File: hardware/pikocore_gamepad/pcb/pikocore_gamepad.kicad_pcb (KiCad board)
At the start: 4 copper layers, 100 x 80 mm, 72 parts, among them J1 PHONES, J4 LCD_FPC, J5 SPEAKER 8R, Q1 2N7002, SW1 DPAD_UP, SW10 BTN_R, SW11 BTN_START, SW12 BTN_SELECT, SW15 PWR, SW2 DPAD_DOWN, SW3 DPAD_LEFT, SW4 DPAD_RIGHT, SW5 BTN_X, SW6 BTN_Y, SW7 BTN_A, SW8 BTN_B, SW9 BTN_L, U1 RP2350-Plus-16MB, U2 TPS61023DRLR, U3 PT2308-S, U4 PAM8302A, U5 PCM5102APWR

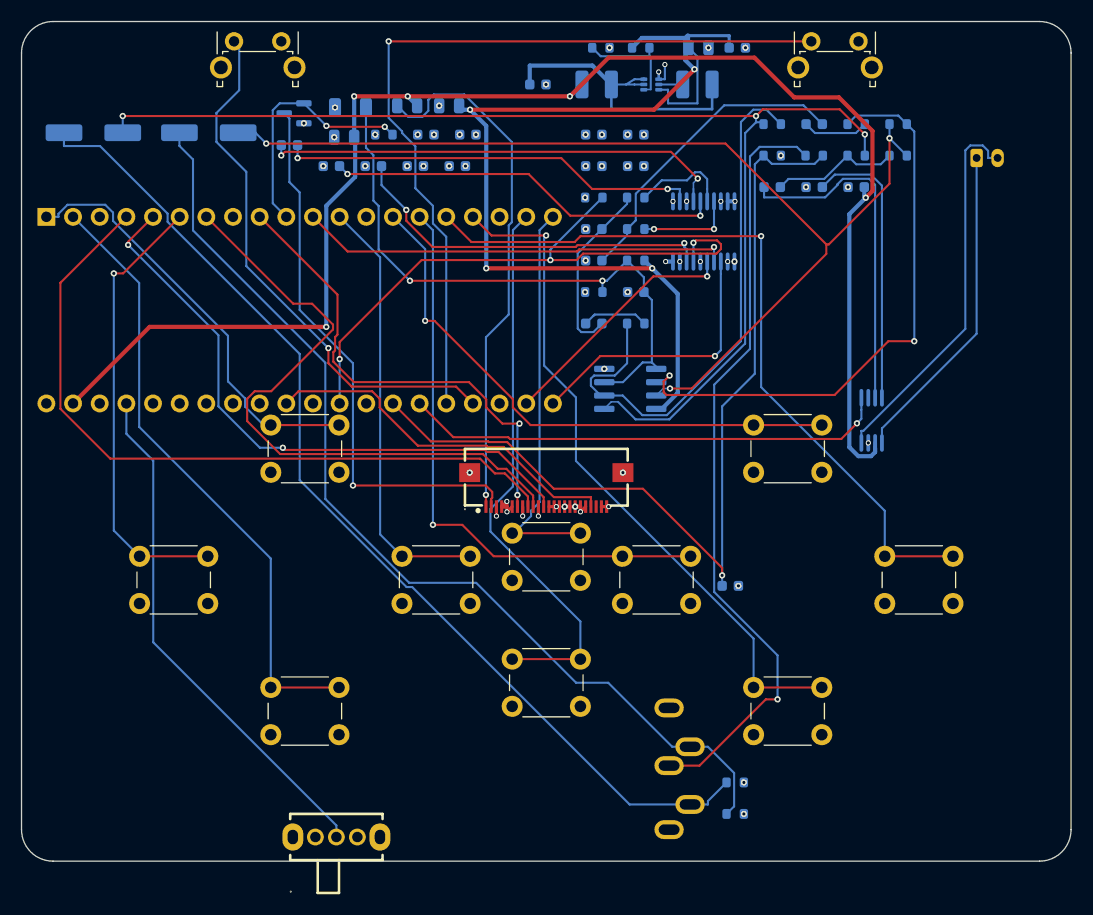
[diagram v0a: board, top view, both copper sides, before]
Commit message: hw: frente Micro y dorso con el modulo plano en 100x60
Frente portado de hw/chipdown-rp2350 (LCD1, J4, SW1-SW15). Dorso: U1 en
MODULE_POS (50,33) rot 0 con flip (pad 1 hacia el borde inferior, USB-C
abajo), J6/J7 arriba en x 33/67, J1 por el borde izquierdo (3,45) rot 270,
MIDI, audio y 470uF en las franjas libres, y el lazo del boost movido
rigido (+29,+50). FREE_REGIONS nuevas para 100x60, fuera de MODULE_BOX.

check_placement.py marca pads pasantes bajo el modulo (TACTO BAJO EL
MODULO). plane_vias.py no pone vias dentro de areas que las prohiben (los
keepouts de los pads de prueba del modulo, detras de J4).

Co-Authored-By: Claude Opus 5.5 <noreply@anthropic.com>
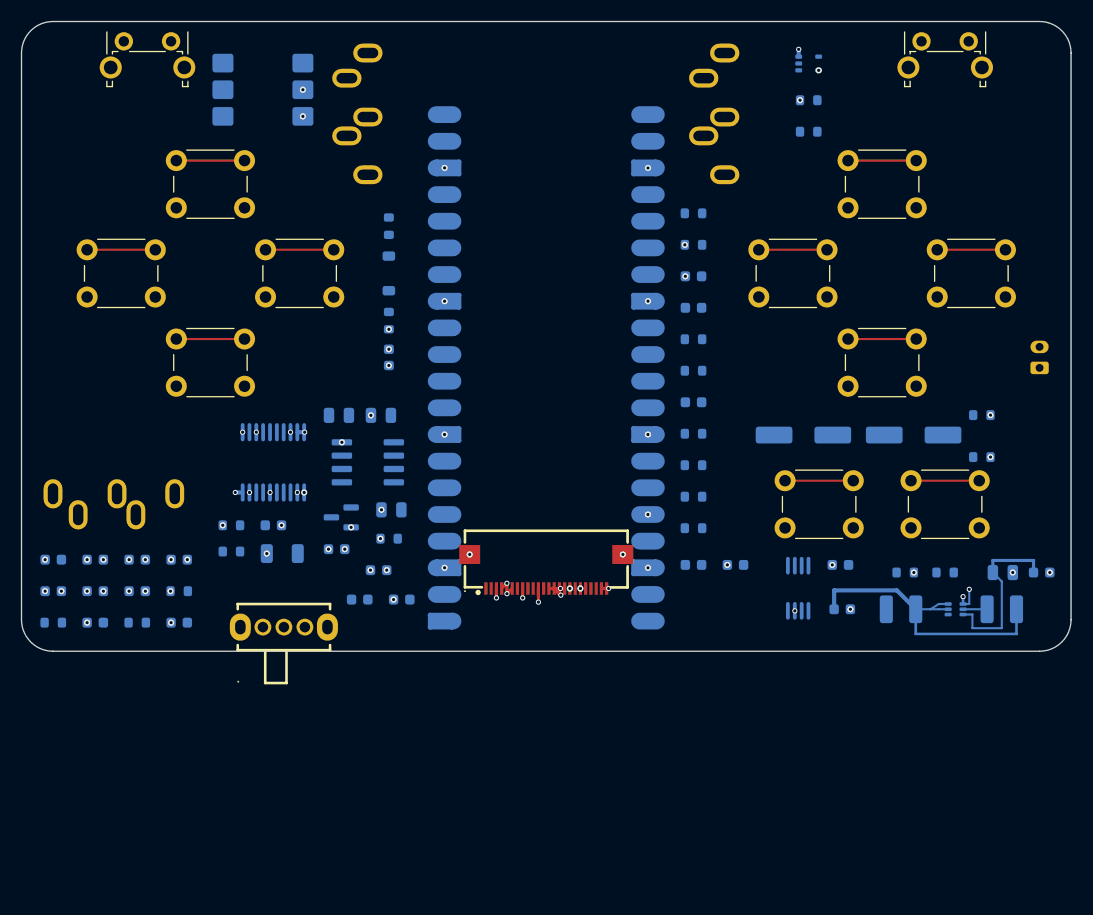
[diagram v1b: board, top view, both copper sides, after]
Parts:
- added C56: 100nF, Capacitor_SMD:C_0603_1608Metric, B.Cu at (35.0, 32.0)
- added D3: 1N4148W, Diode_SMD:D_SOD-123, B.Cu at (35.0, 24.0)
- added J6: MIDI IN, Connector_Audio:Jack_3.5mm_CUI_SJ1-3535NG_Horizontal, B.Cu at (33.0, 3.00)
- added J7: MIDI OUT, Connector_Audio:Jack_3.5mm_CUI_SJ1-3535NG_Horizontal, B.Cu at (67.0, 3.00)
- added R40: 33R, Resistor_SMD:R_0603_1608Metric, B.Cu at (75.0, 7.50)
- added R41: 10R, Resistor_SMD:R_0603_1608Metric, B.Cu at (75.0, 10.5)
- added R42: 220R, Resistor_SMD:R_0603_1608Metric, B.Cu at (35.0, 19.5)
- added R43: 4.7k, Resistor_SMD:R_0603_1608Metric, B.Cu at (35.0, 28.5)
- added U10: H11L1SR2M, Package_DIP:SMDIP-6_W7.62mm, B.Cu at (23.0, 6.50)
- added U9: SN74LVC1G17DCKR, Package_TO_SOT_SMD:SOT-353_SC-70-5, B.Cu at (75.0, 4.00)
- U1: footprint gamesetup_fp:RP2350-Plus_Socket -> gamesetup_fp:RP2350-Plus_Castellated
- moved C23 73.5 mm to (74.5, 39.4), turned to 0 degrees
- moved C24 73.1 mm to (85.0, 39.4), turned to 0 degrees
- moved C14 70.5 mm to (3.02, 54.3)
- moved R7 68.7 mm to (3.02, 57.3)
- moved R18 67.1 mm to (20.0, 50.5), turned to 0 degrees
- moved J1 66.9 mm to (3.00, 45.0), turned to -90 degrees
- moved C15 62.4 mm to (7.03, 54.3)
- moved C16 62.4 mm to (11.0, 54.3)
- moved R15 62.4 mm to (20.0, 48.0), turned to 0 degrees
- moved C17 60.5 mm to (7.03, 57.3)
- moved R8 60.5 mm to (11.0, 57.3)
- moved C4 57.8 mm to (78.2, 56.0)
- moved C5 57.8 mm to (93.5, 52.5)
- moved C7 57.8 mm to (97.2, 52.5)
- moved L1 57.8 mm to (93.4, 56.0)
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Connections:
- U1 pad 32: EXP_GP27 -> MIDI_RX
- U1 pad 34: EXP_GP28 -> MIDI_TX
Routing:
- net VSYS: track 143.0 -> 0.00 mm, vias 5 -> 0
- net AUDIO_L: track 115.9 -> 0.00 mm, vias 3 -> 0
- net AUDIO_R: track 99.6 -> 0.00 mm, vias 3 -> 0
- net JACK_L: track 99.0 -> 0.00 mm
- net JACK_R: track 94.6 -> 0.00 mm
- net JACK_DET: track 87.5 -> 0.00 mm, vias 1 -> 0
- net 5V: track 98.4 -> 16.8 mm, vias 4 -> 0
- net BTN_R: track 77.0 -> 0.00 mm, vias 1 -> 0
- net JACK_DETSW: track 74.6 -> 0.00 mm, vias 1 -> 0
- net LCD_SCK: track 69.9 -> 0.00 mm
- net BTN_A: track 73.1 -> 6.50 mm, vias 1 -> 0
- net LCD_DC: track 61.1 -> 0.00 mm
- net BTN_B: track 65.6 -> 6.50 mm, vias 1 -> 0
- net DAC_XSMT: track 59.0 -> 0.00 mm, vias 3 -> 0
- net LCD_MOSI: track 58.1 -> 0.00 mm, vias 2 -> 0
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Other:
- board size 100 x 80 mm -> 100 x 60 mm

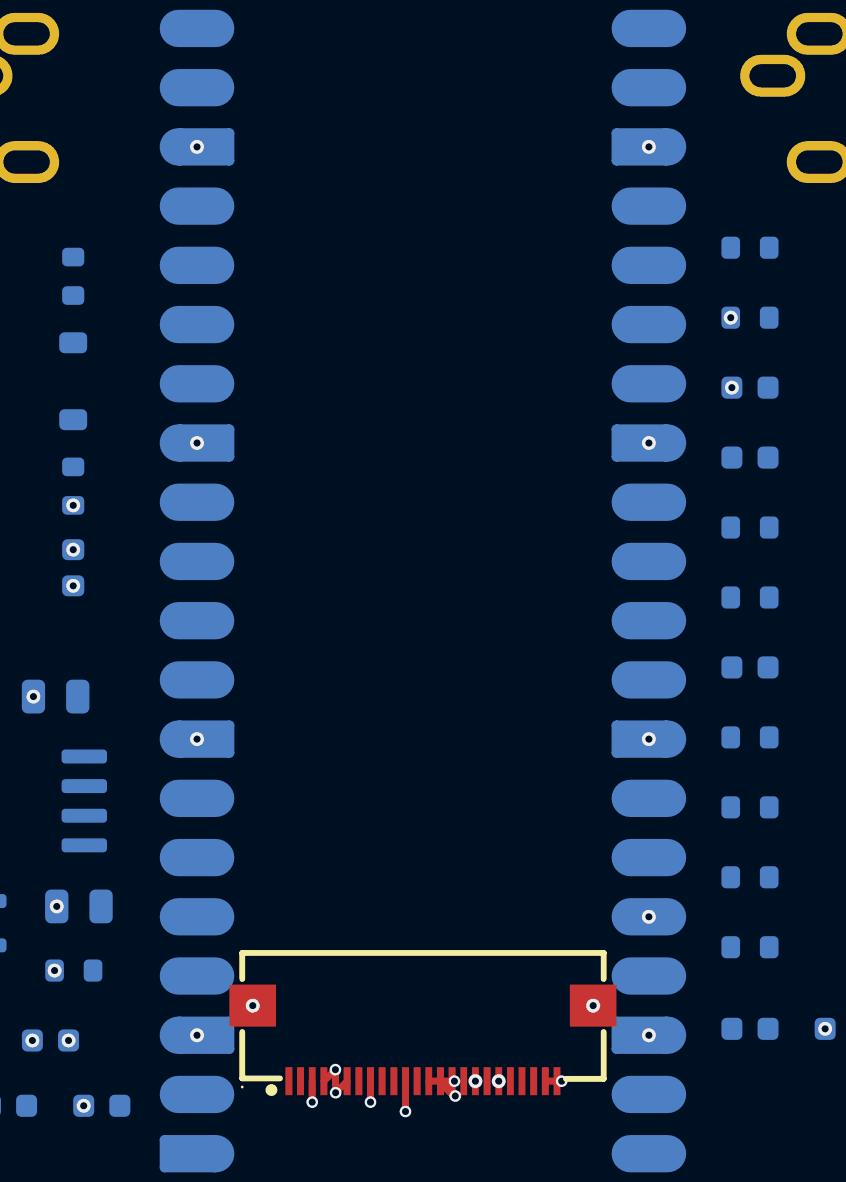
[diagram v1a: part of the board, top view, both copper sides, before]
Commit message: hw: sin vias ni pasta bajo las pastillas del modulo
plane_vias.py ya no pone via en las pastillas de U1 (se sueldan a mano y
el taladro chupa el estano): la via va afuera de la caja de sus pastillas,
a 0.3mm del cobre, unida por un tramo en B.Cu. check_placement.py falla si
una via toca una pastilla de U1.

gen_fp.py quita la pasta sin nombre que la huella oficial traia para
D1-D3 (bajo el modulo el esten imprimiria bolitas). Test de las 40 pastas.

Esquematico y netlist regenerados (U1 ya con la huella castellated).

Co-Authored-By: Claude Opus 5.5 <noreply@anthropic.com>
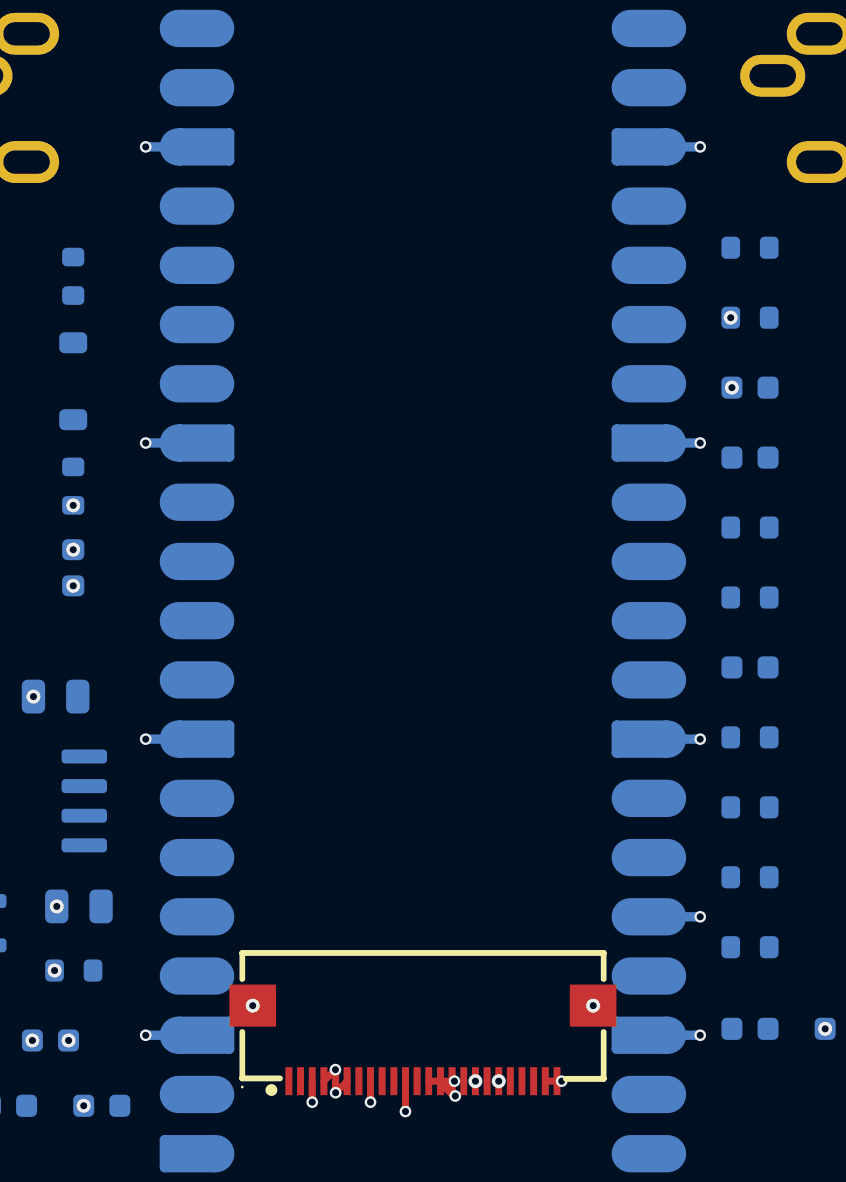
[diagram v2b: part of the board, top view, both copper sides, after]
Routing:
- net GND: track 9.89 -> 27.5 mm
- net 3V3: track 2.10 -> 4.30 mm

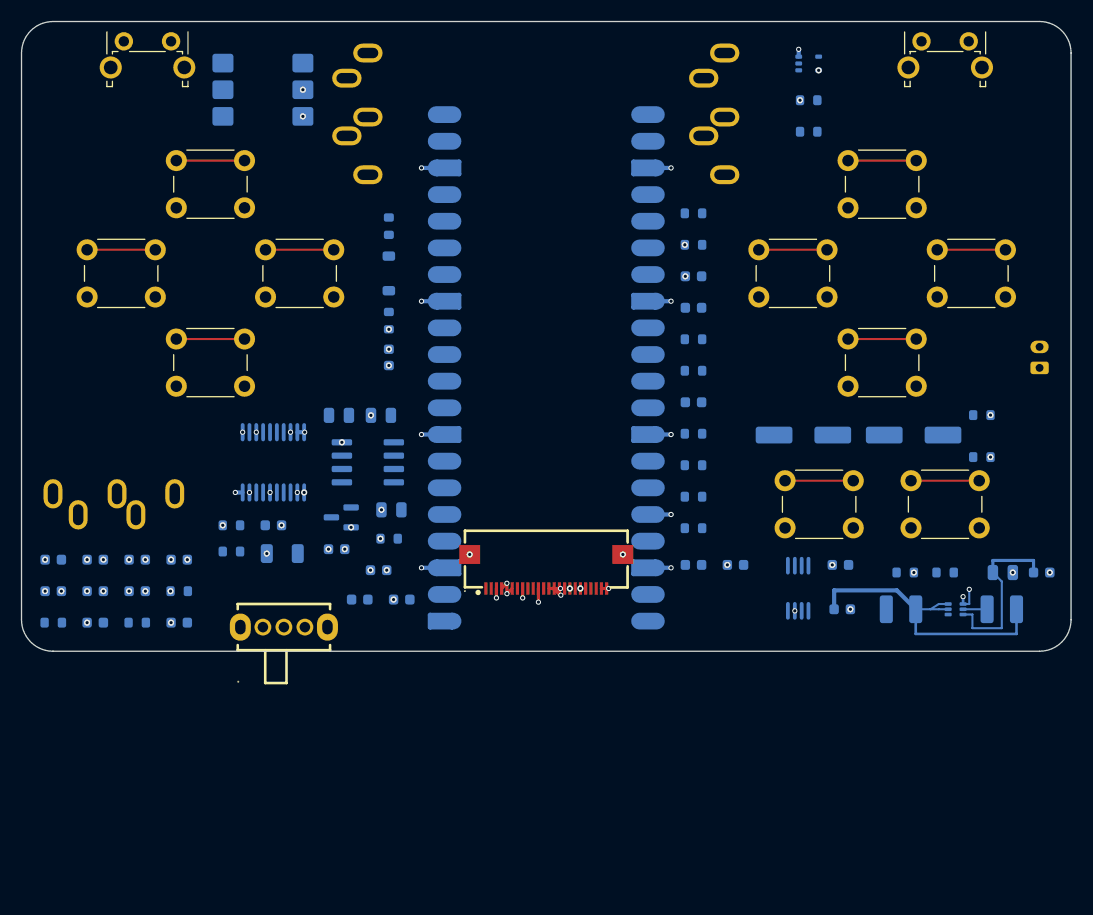
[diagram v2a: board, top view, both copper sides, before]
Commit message: hw: ruteo de la placa con modulo (DRC 0 errores, 0 sin conectar)
Un solo ciclo de route_cycle.sh: freerouting cierra todo en la pasada 1
(696 pistas, 166 vias). DRC: 0 errores, 15 avisos (serigrafia en borde,
lib_footprint_mismatch de SW9/SW10, serigrafia de C23/C24), 0 sin
conectar, 0 de paridad. 5V va en 0.4mm hasta el op-amp sin pista a mano.

check_placement.py mide la via contra la pastilla de U1 como circulo
contra rectangulo: la caja inflada daba falso positivo en las esquinas
(via de BTN_Y a 0.07mm del extremo interior de U1.15, sin tocarla).

Co-Authored-By: Claude Opus 5.5 <noreply@anthropic.com>
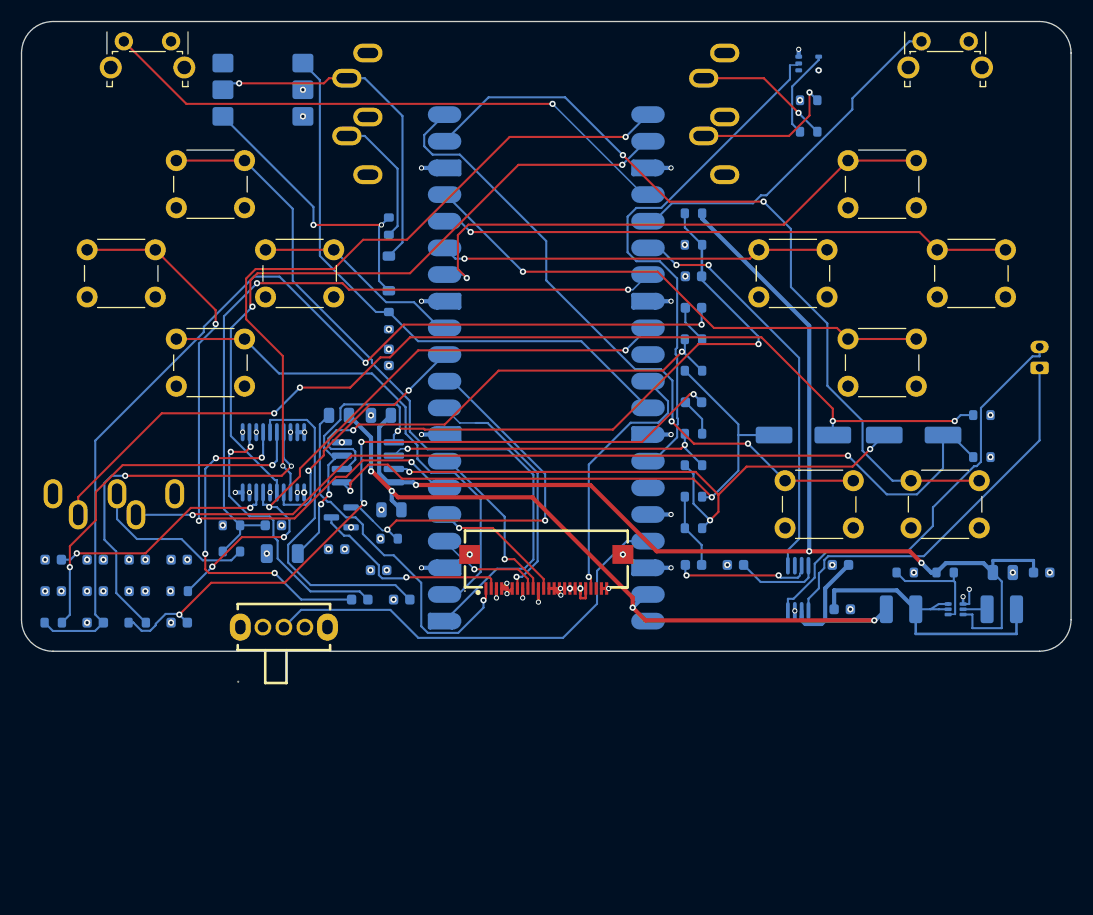
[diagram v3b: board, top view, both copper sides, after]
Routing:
- net 5V: track 16.8 -> 122.4 mm, vias 0 -> 3
- net JACK_L: track 0.00 -> 98.8 mm, vias 0 -> 4
- net AOUT_L: track 0.00 -> 95.0 mm, vias 0 -> 2
- net JACK_R: track 0.00 -> 88.7 mm, vias 0 -> 2
- net VREF25: track 0.00 -> 83.0 mm, vias 0 -> 4
- net VSYS: track 0.00 -> 80.7 mm, vias 0 -> 4
- net BTN_START: track 6.50 -> 76.2 mm, vias 0 -> 2
- net AOUT_R: track 0.00 -> 69.6 mm, vias 0 -> 4
- net JACK_DET: track 0.00 -> 68.7 mm, vias 0 -> 2
- net I2S_BCK: track 0.00 -> 66.9 mm, vias 0 -> 2
- net I2S_LRCK: track 0.00 -> 66.4 mm, vias 0 -> 2
- net DPAD_UP: track 6.50 -> 71.3 mm
- net DAC_XSMT: track 0.00 -> 61.0 mm, vias 0 -> 4
- net AUDIO_R: track 0.00 -> 60.2 mm, vias 0 -> 3
- net AUDIO_L: track 0.00 -> 57.9 mm, vias 0 -> 2
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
